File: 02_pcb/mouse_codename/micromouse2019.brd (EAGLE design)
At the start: 45 x 50 mm, 78 parts

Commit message: I2C pull up resistors added
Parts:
- added R1, R2: 4k7, 0-micromouse2019:R0402
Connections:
- net +3V3: now also R1.2, R2.2
- net SCL: now also R1.1
- net SDA: now also R2.1
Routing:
- net +3V3: track 167.0 -> 170.7 mm
- net SDA: track 15.0 -> 16.4 mm
- net SCL: track 15.0 -> 15.8 mm
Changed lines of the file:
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@@
 <attribute name="VALUE" x="29.845" y="26.924" size="0.8128" layer="28" rot="MR0"/>
+</element>
+<element name="R1" library="0-micromouse2019" package="R0402" package3d_urn="urn:adsk.eagle:package:23547/3" value="4k7" x="29.718" y="40.64" smashed="yes" rot="R270">
+<attribute name="NAME" x="28.448" y="41.402" size="0.8128" layer="25" rot="R270"/>
+<attribute name="SPICEPREFIX" value="R" x="29.718" y="40.64" size="1.778" layer="27" rot="R270" display="off"/>
+<attribute name="VALUE" x="28.321" y="41.275" size="0.8128" layer="27" rot="R270"/>
+</element>
+<element name="R2" library="0-micromouse2019" package="R0402" package3d_urn="urn:adsk.eagle:package:23547/3" value="4k7" x="31.115" y="40.64" smashed="yes" rot="MR0">
+<attribute name="NAME" x="31.75" y="41.275" size="0.8128" layer="26" rot="MR0"/>
+<attribute name="SPICEPREFIX" value="R" x="31.115" y="40.64" size="1.778" layer="28" rot="MR0" display="off"/>
+<attribute name="VALUE" x="31.75" y="39.243" size="0.8128" layer="28" rot="MR0"/>
 </element>
 </elements>
@@
 <wire x1="25.14" y1="42.725" x2="24.615" y2="42.2" width="0.1524" layer="1"/>
 <wire x1="23.4" y1="42.2" x2="24.05" y2="42.2" width="0.3" layer="16"/>
+<contactref element="R1" pad="2"/>
+<contactref element="R2" pad="2"/>
+<wire x1="30.615" y1="39.628675" x2="29.73" y2="38.743675" width="0.1524" layer="16"/>
+<wire x1="29.73" y1="38.69" x2="29.73" y2="38.743675" width="0.1524" layer="16"/>
+<wire x1="30.615" y1="39.628675" x2="30.615" y2="40.64" width="0.1524" layer="16"/>
+<wire x1="29.718" y1="40.14" x2="29.718" y2="38.702" width="0.127" layer="1"/>
+<wire x1="29.718" y1="38.702" x2="29.73" y2="38.69" width="0.127" layer="1"/>
 </signal>
 <signal name="VCC">
@@
 <wire x1="31.1" y1="37.2" x2="31.1" y2="38.43" width="0.1524" layer="1"/>
 <wire x1="31.1" y1="38.43" x2="30.56" y2="38.97" width="0.1524" layer="1"/>
-<wire x1="30.56" y1="46.04" x2="30.56" y2="38.97" width="0.1524" layer="1"/>
+<wire x1="30.56" y1="46.04" x2="30.56" y2="41.148" width="0.1524" layer="1"/>
 <contactref element="MCU:IC1" pad="61"/>
 <contactref element="IMU:IC1" pad="23"/>
+<wire x1="30.56" y1="41.148" x2="30.56" y2="38.97" width="0.1524" layer="1"/>
 <wire x1="28.365" y1="46.922" x2="29.678" y2="46.922" width="0.1524" layer="1"/>
 <wire x1="29.678" y1="46.922" x2="30.56" y2="46.04" width="0.1524" layer="1"/>
+<contactref element="R1" pad="1"/>
+<wire x1="30.552" y1="41.14" x2="30.56" y2="41.148" width="0.127" layer="1"/>
+<wire x1="29.718" y1="41.14" x2="30.552" y2="41.14" width="0.127" layer="1"/>
+<wire x1="30.552" y1="41.14" x2="30.56" y2="41.148" width="0.127" layer="1"/>
 </signal>
 <signal name="SDA">
@@
 <contactref element="IMU:IC1" pad="24"/>
 <wire x1="28.365" y1="47.422" x2="29.938" y2="47.422" width="0.1524" layer="1"/>
+<contactref element="R2" pad="1"/>
+<wire x1="31.615" y1="40.64" x2="31.615" y2="39.935" width="0.1524" layer="16"/>
+<wire x1="31.615" y1="39.935" x2="31.08" y2="39.4" width="0.1524" layer="16"/>
 </signal>
 <signal name="UART3_TX">

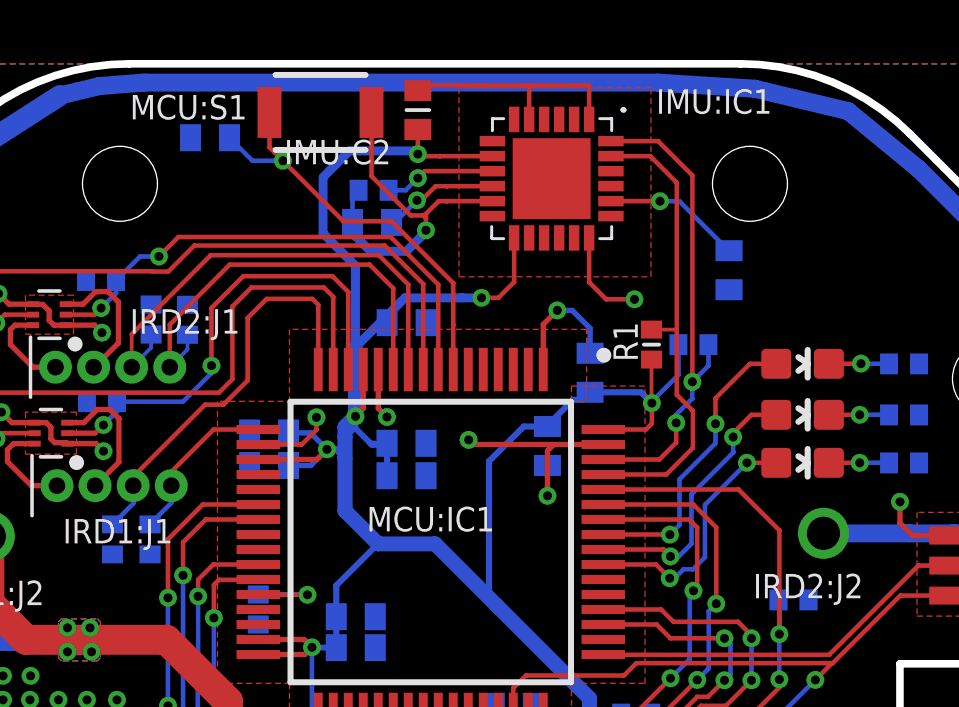
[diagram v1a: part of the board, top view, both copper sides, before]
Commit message: I2C pull up R on bottom & GND connection
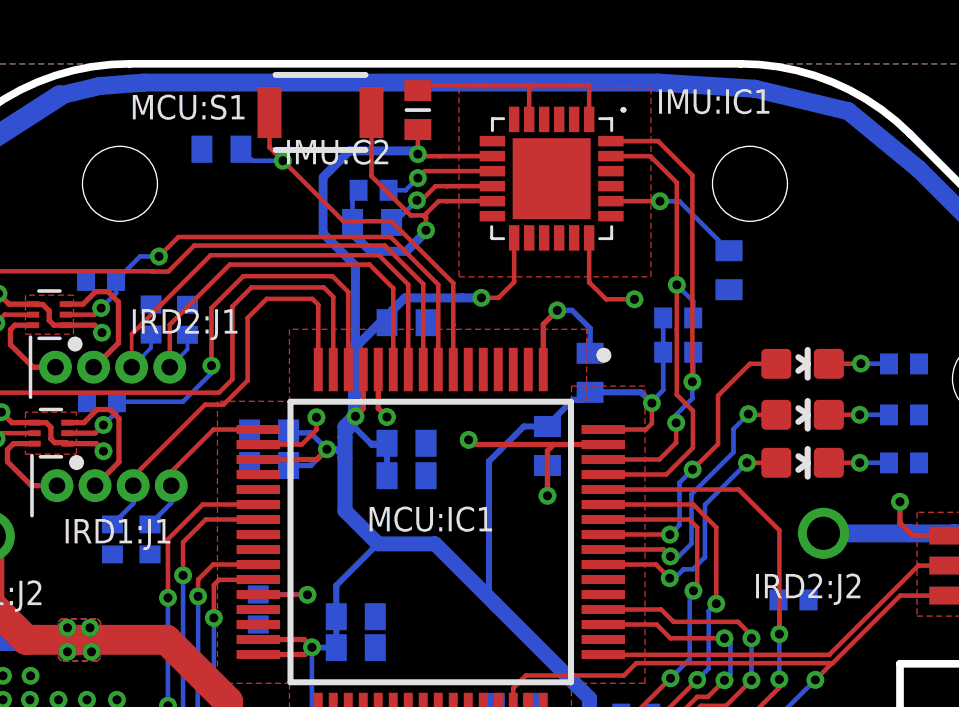
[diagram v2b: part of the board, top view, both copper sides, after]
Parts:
- moved R1 1.26 mm to (30.6, 41.5), flipped to the bottom, turned to 0 degrees
- moved R2 0.57 mm to (30.6, 40.4)
- moved MCU:C11 0.54 mm to (15.4, 47.2)
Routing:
- net +3V3: track 170.7 -> 170.0 mm
- net MCU:NRST: track 14.1 -> 13.6 mm
- net SCL: track 15.8 -> 16.3 mm, vias 0 -> 1

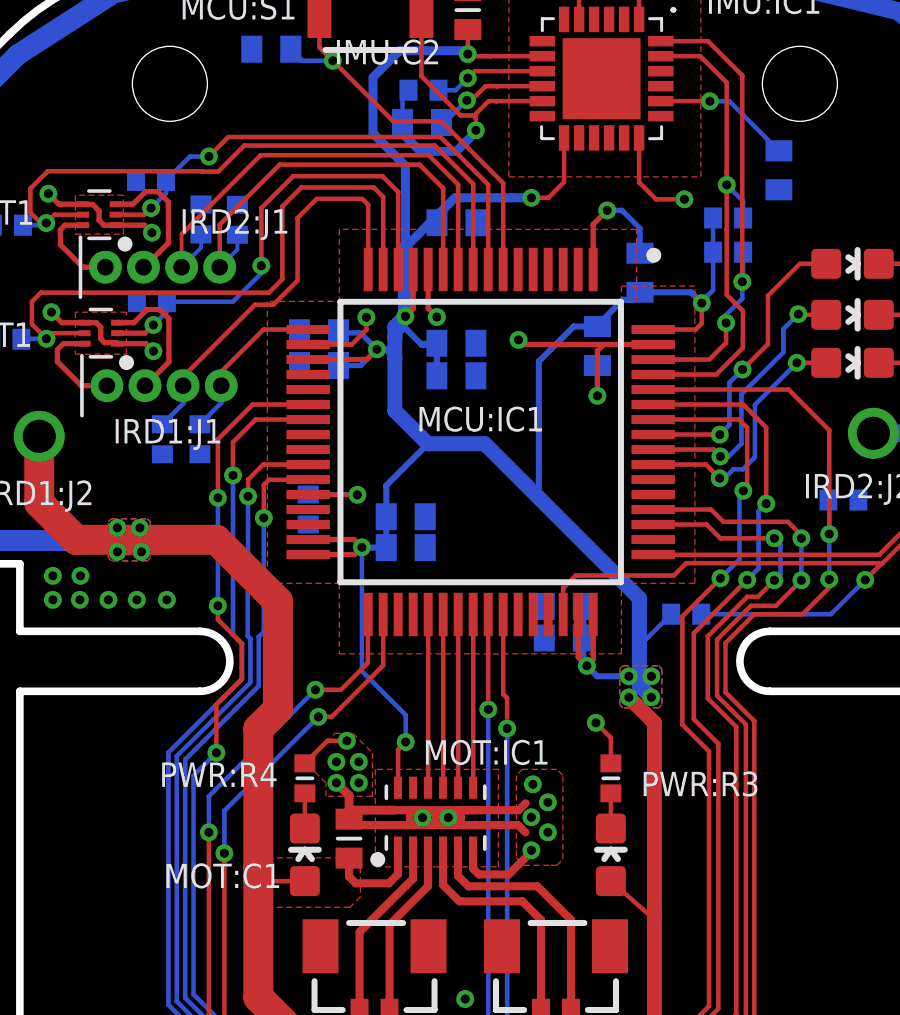
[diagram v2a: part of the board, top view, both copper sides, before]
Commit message: DRV Nsleep Vcc connect
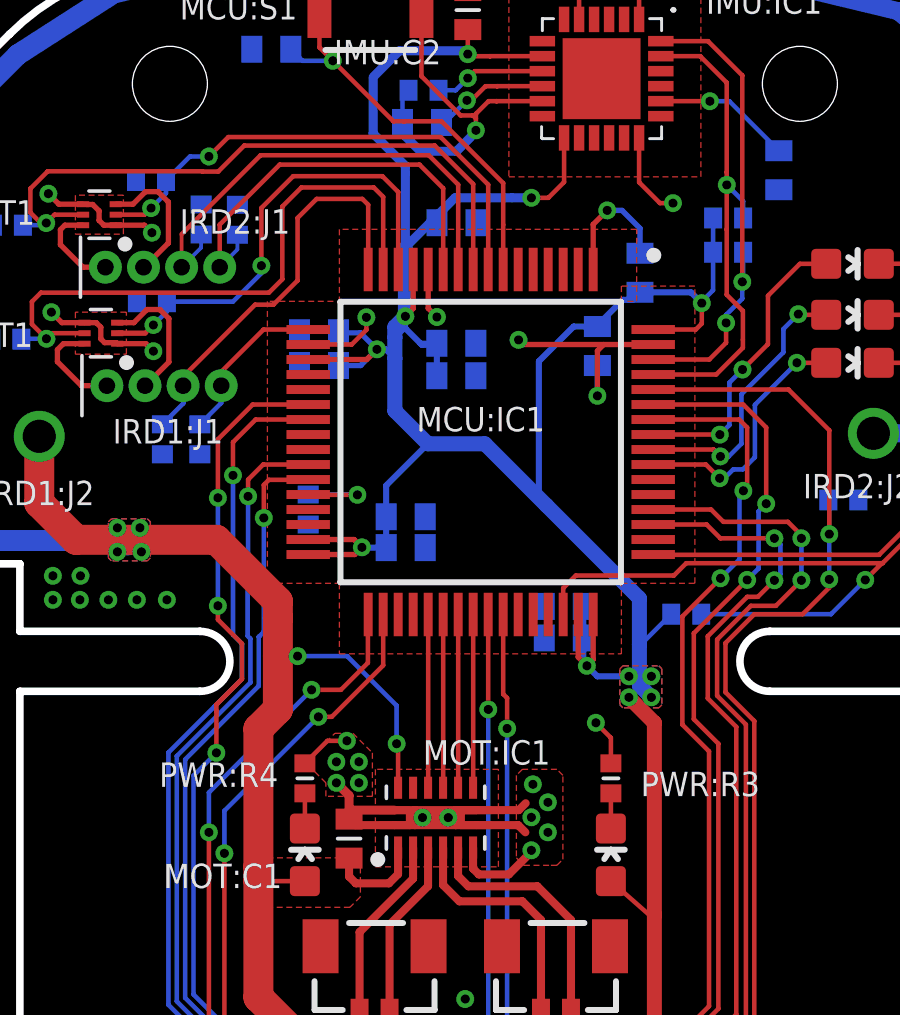
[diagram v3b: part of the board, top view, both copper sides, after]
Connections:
- net +3V3: no longer MOT:IC1.12
- net VCC: now also MOT:IC1.12
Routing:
- net +3V3: track 170.0 -> 161.2 mm, vias 16 -> 15
- net VCC: track 118.7 -> 126.1 mm, vias 4 -> 6
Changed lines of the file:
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@@
 <drawing>
 <settings>
-<setting alwaysvectorfont="no"/>
+<setting alwaysvectorfont="yes"/>
 <setting verticaltext="up"/>
 </settings>
-<grid distance="5" unitdist="mil" unit="mm" style="lines" multiple="1" display="yes" altdistance="0.01" altunitdist="mm" altunit="mm"/>
+<grid distance="5" unitdist="mil" unit="mil" style="lines" multiple="1" display="yes" altdistance="0.01" altunitdist="mm" altunit="mm"/>
 <layers>
 <layer number="1" name="Top" color="4" fill="1" visible="yes" active="yes"/>
@@
 </layers>
 <board>
-<fusionsync huburn="a.cGVyc29uYWw6dWUyOWUzYzUy" projecturn="a.cGVyc29uYWw6dWUyOWUzYzUyIzIwMTkwMjExMTc1NjcyODUx" f3durn="urn:adsk.wipprod:dm.lineage:jzhWZ2RJTSK-yRQwBFZECw" pcbguid="c2b5e295-5b88-443b-b552-b85fb43e7534" lastpulledtime="2019-02-22T16:16:36Z" lastsyncedchangeguid="98a80c0f-199f-95f9-b975-eea7380629f9"/>
+<fusionsync huburn="a.cGVyc29uYWw6dWUyOWUzYzUy" projecturn="a.cGVyc29uYWw6dWUyOWUzYzUyIzIwMTkwMjExMTc1NjcyODUx" f3durn="urn:adsk.wipprod:dm.lineage:jzhWZ2RJTSK-yRQwBFZECw" pcbguid="c2b5e295-5b88-443b-b552-b85fb43e7534" lastpulledtime="2019-02-22T16:16:36Z" lastsyncedchangeguid="9baeba4e-d521-f71b-b12c-e54dc2902a2e"/>
 <plain>
 <rectangle x1="6.858" y1="11.303" x2="13.589" y2="27.813" layer="39"/>
@@
 <contactref element="MCU:IC1" pad="33"/>
 <via x="13.3" y="21.05" extent="1-16" drill="0.3" diameter="0.6"/>
-<wire x1="13.3" y1="21.05" x2="13.3" y2="22.25" width="0.1524" layer="16"/>
-<via x="16.85" y="25.8" extent="1-16" drill="0.3" diameter="0.6"/>
-<wire x1="16.85" y1="25.8" x2="17.7" y2="25.8" width="0.1524" layer="1"/>
+<wire x1="13.3" y1="21.05" x2="13.3" y2="22.377" width="0.1524" layer="16"/>
+<via x="16.723" y="25.8" extent="1-16" drill="0.3" diameter="0.6"/>
+<wire x1="16.723" y1="25.8" x2="17.7" y2="25.8" width="0.1524" layer="1"/>
 <wire x1="17.7" y1="25.8" x2="18.6" y2="26.7" width="0.1524" layer="1"/>
 <wire x1="18.6" y1="26.7" x2="18.6" y2="28.3" width="0.1524" layer="1"/>
 <wire x1="18.6" y1="28.3" x2="18.61" y2="28.31" width="0.1524" layer="1"/>
 <wire x1="13.3" y1="14.142" x2="13.3" y2="21.05" width="0.1524" layer="1"/>
-<wire x1="13.3" y1="22.25" x2="16.85" y2="25.8" width="0.1524" layer="16"/>
+<wire x1="13.3" y1="22.377" x2="16.723" y2="25.8" width="0.1524" layer="16"/>
 <wire x1="3.66" y1="6.27" x2="3.45" y2="6.06" width="0.1524" layer="16"/>
 <wire x1="3.45" y1="6.06" x2="2.51" y2="6.06" width="0.1524" layer="16"/>
@@
 <wire x1="9.6973" y1="37.49856875" x2="9.82376875" y2="37.3721" width="0.1778" layer="1"/>
 <wire x1="27.64" y1="44.197" x2="27.64" y2="42.718" width="0.1524" layer="1"/>
-<wire x1="27.64" y1="42.718" x2="28.208" y2="42.15" width="0.1524" layer="1"/>
+<wire x1="27.64" y1="42.718" x2="28.335" y2="42.023" width="0.1524" layer="1"/>
 <wire x1="24.415" y1="45.422" x2="22.892" y2="45.422" width="0.1524" layer="1"/>
 <wire x1="22.892" y1="45.422" x2="22.89" y2="45.42" width="0.1524" layer="1"/>
@@
 <wire x1="20.385" y1="46.2533625" x2="21.69238125" y2="44.94598125" width="0.1524" layer="1"/>
 <wire x1="20.385" y1="48.379" x2="20.385" y2="46.2533625" width="0.1524" layer="1"/>
-<wire x1="28.208" y1="42.15" x2="29.15" y2="42.15" width="0.1524" layer="1"/>
-<via x="29.15" y="42.15" extent="1-16" drill="0.3" diameter="0.6"/>
+<wire x1="28.335" y1="42.023" x2="28.769" y2="42.023" width="0.1524" layer="1"/>
+<via x="28.769" y="42.023" extent="1-16" drill="0.3" diameter="0.6"/>
 <wire x1="25.64" y1="49.22" x2="25.64" y2="48.147" width="0.1524" layer="1"/>
 <wire x1="27.64" y1="49.28" x2="27.64" y2="48.147" width="0.1524" layer="1"/>
@@
 <via x="29.73" y="38.69" extent="1-16" drill="0.3" diameter="0.6"/>
 <contactref element="PWR:LED1" pad="A"/>
-<contactref element="MOT:IC1" pad="12"/>
-<via x="19.86" y="24.06" extent="1-16" drill="0.3" diameter="0.6"/>
 <wire x1="23.46" y1="4.58" x2="24.63" y2="4.58" width="0.5" layer="1"/>
 <wire x1="24.63" y1="4.58" x2="25.15" y2="5.1" width="0.5" layer="1"/>
@@
 <contactref element="EPL:PORT1" pad="P3"/>
 <contactref element="PWR:LDO1" pad="1"/>
-<wire x1="19.606" y1="22.5356" x2="19.606" y2="23.806" width="0.1524" layer="1"/>
-<wire x1="19.606" y1="23.806" x2="19.86" y2="24.06" width="0.1524" layer="1"/>
 <wire x1="28.15" y1="18.3" x2="27.976834375" y2="18.3" width="0.1524" layer="1"/>
 <wire x1="27.976834375" y1="18.3" x2="26.7" y2="19.423" width="0.1524" layer="1"/>
@@
 <wire x1="38.19" y1="3.71" x2="38.2" y2="3.7" width="0.1524" layer="16"/>
 <wire x1="28.15" y1="18.3" x2="28.15" y2="24.7" width="0.5" layer="1"/>
-<wire x1="19.86" y1="24.06" x2="19.86" y2="24.96" width="0.1524" layer="16"/>
-<wire x1="19.86" y1="24.96" x2="18.4" y2="26.42" width="0.1524" layer="16"/>
 <wire x1="20.11" y1="39.81" x2="20.11" y2="38.51" width="0.1778" layer="1"/>
 <wire x1="20.11" y1="38.51" x2="19.85" y2="38.25" width="0.1778" layer="1"/>
@@
 <via x="18.4" y="30.55" extent="1-16" drill="0.3" diameter="0.6"/>
 <wire x1="16.61" y1="30.81" x2="18.14" y2="30.81" width="0.1778" layer="1"/>
-<wire x1="18.4" y1="26.42" x2="18.4" y2="30.55" width="0.1524" layer="16"/>
 <wire x1="18.4" y1="30.55" x2="18.14" y2="30.81" width="0.1778" layer="1"/>
 <wire x1="18.41" y1="30.54" x2="18.4" y2="30.55" width="0.1778" layer="16"/>
@@
 <wire x1="14.95" y1="19.9" x2="14.95" y2="24.5" width="1" layer="1"/>
 <wire x1="14.95" y1="24.5" x2="15.6" y2="25.15" width="1" layer="1"/>
-<wire x1="15.6" y1="25.15" x2="15.6" y2="28.75" width="1" layer="1"/>
+<wire x1="15.6" y1="25.15" x2="15.6" y2="26.924" width="1" layer="1"/>
+<wire x1="15.6" y1="26.924" x2="15.6" y2="28.194" width="1" layer="1"/>
+<wire x1="15.6" y1="28.194" x2="15.6" y2="28.75" width="1" layer="1"/>
 <wire x1="16.35" y1="11.45" x2="16.35" y2="14.15" width="1" layer="1"/>
 <wire x1="13.55" y1="30.8" x2="15.6" y2="28.75" width="1" layer="1"/>
@@
 <wire x1="16.5" y1="19.423" x2="14.958" y2="19.423" width="0.1524" layer="1"/>
 <wire x1="14.958" y1="19.423" x2="14.95" y2="19.431" width="0.1524" layer="1"/>
+<contactref element="MOT:IC1" pad="12"/>
+<via x="16.256" y="26.924" extent="1-16" drill="0.3" diameter="0.6"/>
+<via x="19.558" y="24.003" extent="1-16" drill="0.3" diameter="0.6"/>
+<wire x1="19.606" y1="22.5356" x2="19.606" y2="23.955" width="0.1524" layer="1"/>
+<wire x1="19.606" y1="23.955" x2="19.558" y2="24.003" width="0.1524" layer="1"/>
+<wire x1="19.558" y1="24.003" x2="19.558" y2="25.273" width="0.1524" layer="16"/>
+<wire x1="19.558" y1="25.273" x2="17.907" y2="26.924" width="0.1524" layer="16"/>
+<wire x1="17.907" y1="26.924" x2="16.256" y2="26.924" width="0.1524" layer="16"/>
+<wire x1="16.256" y1="26.924" x2="15.6" y2="26.924" width="0.1524" layer="1"/>
 </signal>
 <signal name="SCL">

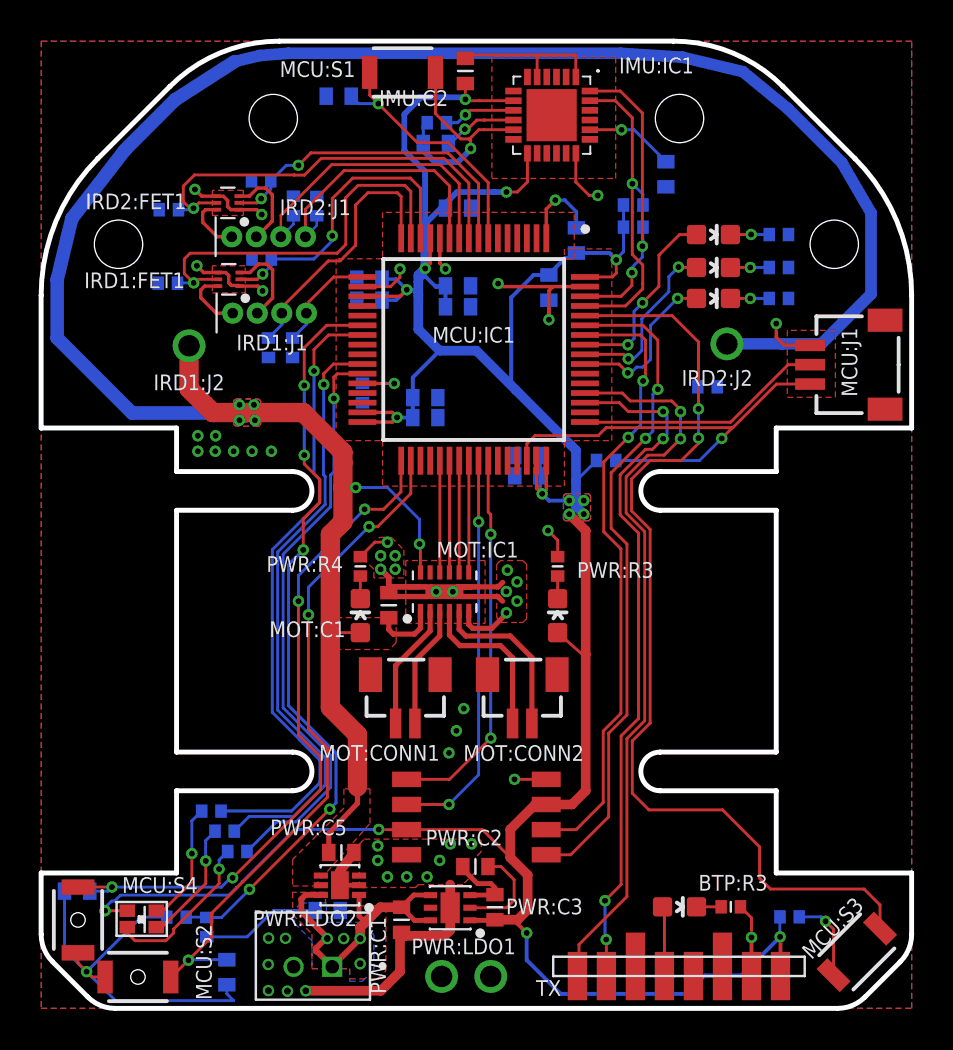
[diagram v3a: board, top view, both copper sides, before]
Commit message: IMU EP removed & MCU_C11 & GND plane position adjustments
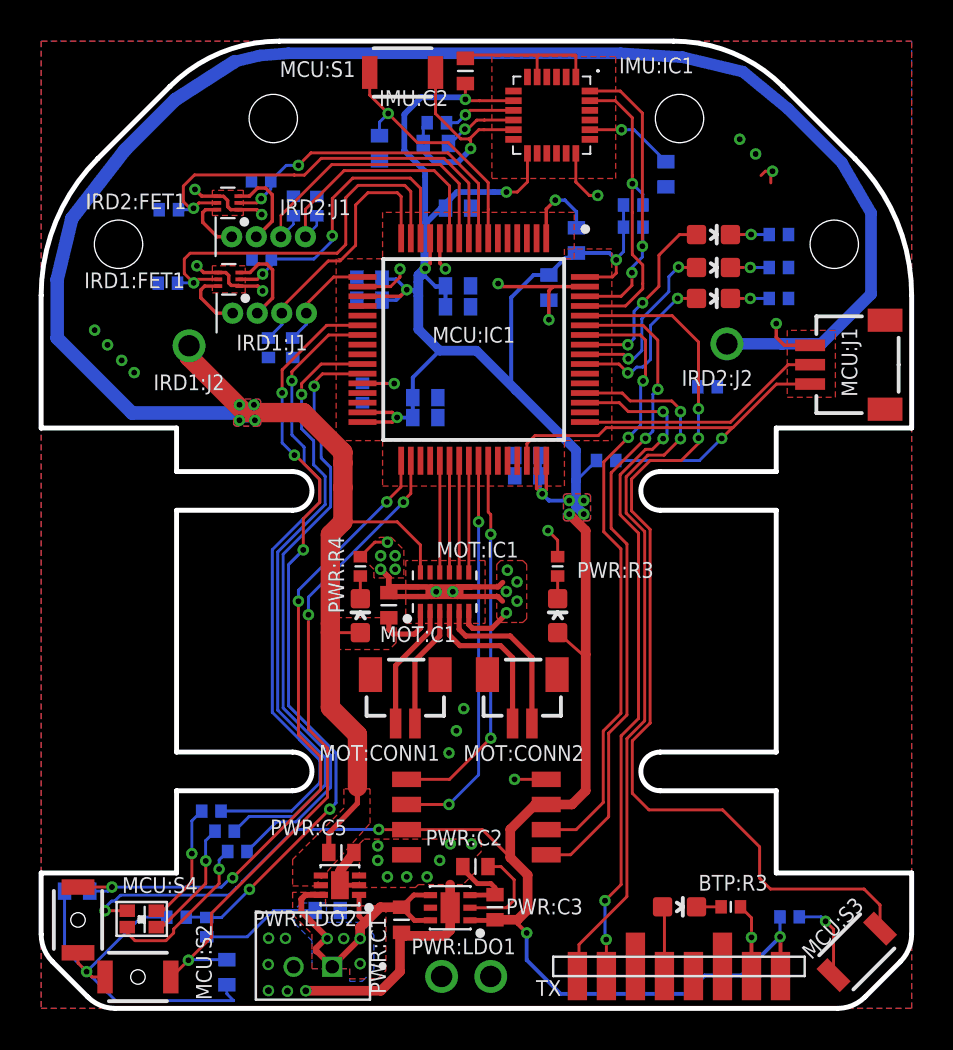
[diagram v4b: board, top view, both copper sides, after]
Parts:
- moved MCU:C11 3.42 mm to (17.5, 44.5), turned to 270 degrees
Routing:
- net VCC: track 126.1 -> 122.5 mm, vias 6 -> 4
- net GND: track 115.9 -> 117.3 mm
- net MCU:RGB_G: track 31.2 -> 32.5 mm
- net MCU:RGB_B: track 30.6 -> 31.7 mm
- net V_BAT_LEVEL: track 39.3 -> 40.2 mm
- net MCU:RGB_R: track 33.1 -> 34.0 mm
- net MCU:BTN2: track 36.1 -> 35.6 mm
